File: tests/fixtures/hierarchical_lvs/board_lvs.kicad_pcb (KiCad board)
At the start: 2 copper layers, 2 parts

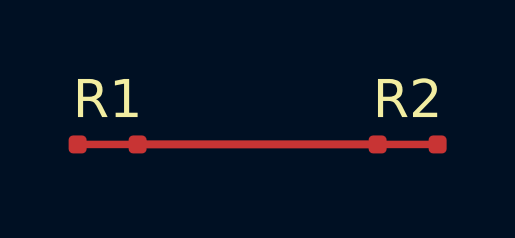
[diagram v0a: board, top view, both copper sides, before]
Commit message: test(lvs): separate hierarchical fixture power routes
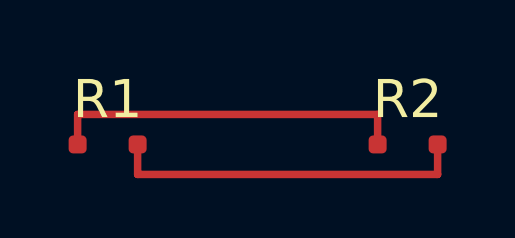
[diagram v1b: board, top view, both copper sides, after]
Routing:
- net VCC: track 10.0 -> 12.0 mm
- net GND: track 10.0 -> 12.0 mm
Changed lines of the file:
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@@
       (roundrect_rratio 0.25) (net 2 "GND"))
   )
-  (segment (start 99 100) (end 109 100) (width 0.25) (layer "F.Cu") (net 1)
+  (segment (start 99 100) (end 99 99) (width 0.25) (layer "F.Cu") (net 1)
     (uuid "hlvs-seg-vcc"))
-  (segment (start 101 100) (end 111 100) (width 0.25) (layer "F.Cu") (net 2)
+  (segment (start 99 99) (end 109 99) (width 0.25) (layer "F.Cu") (net 1)
+    (uuid "hlvs-seg-vcc-middle"))
+  (segment (start 109 99) (end 109 100) (width 0.25) (layer "F.Cu") (net 1)
+    (uuid "hlvs-seg-vcc-end"))
+  (segment (start 101 100) (end 101 101) (width 0.25) (layer "F.Cu") (net 2)
     (uuid "hlvs-seg-gnd"))
+  (segment (start 101 101) (end 111 101) (width 0.25) (layer "F.Cu") (net 2)
+    (uuid "hlvs-seg-gnd-middle"))
+  (segment (start 111 101) (end 111 100) (width 0.25) (layer "F.Cu") (net 2)
+    (uuid "hlvs-seg-gnd-end"))
 )
